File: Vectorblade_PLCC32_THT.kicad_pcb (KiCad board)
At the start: 2 copper layers, 47.2 x 46.9 mm, 12 parts, among them CON3 EDGE-CONNECTOR, U1 SST39SF020, U2 74AHC1G04, U3 74AHC1G08

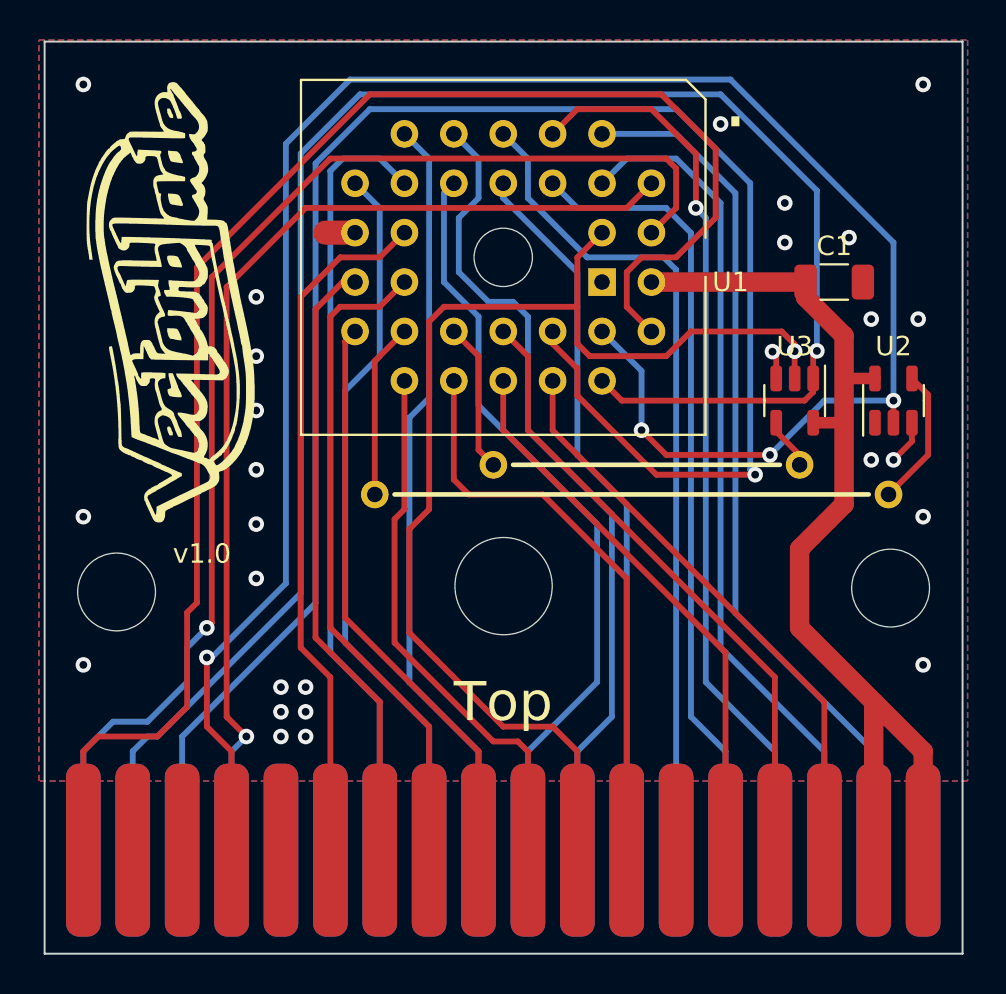
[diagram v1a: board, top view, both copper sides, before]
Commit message: Correct CE error
Correct CE schematic and board error
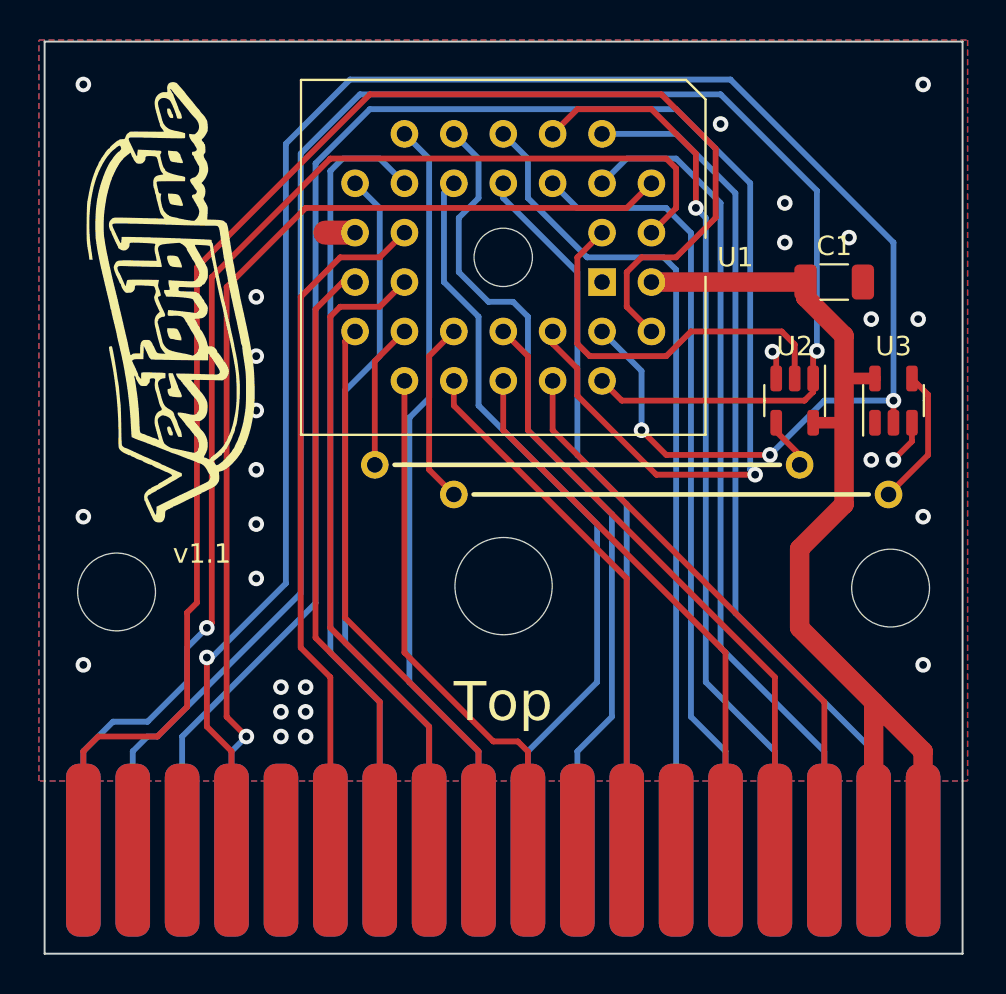
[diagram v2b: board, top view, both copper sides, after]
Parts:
- U2: value 74AHC1G04 -> 74AHC1G08
- U3: value 74AHC1G08 -> 74AHC1G04
- moved U2 5.08 mm to (172.5, 91.2), turned to -90 degrees
- moved U3 5.08 mm to (177.5, 91.2), turned to 90 degrees
- moved ? 2.54 mm to (154.9, 96.0)
- moved ? 1.52 mm to (150.9, 94.5)
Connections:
- ? pad 22: Net-(U1-Pad22) -> /~{CE}
- ? pad 22: Net-(U1-Pad22) -> /~{OE}
- ? pad 24: Net-(U1-Pad24) -> /~{OE}
- ? pad 24: Net-(U1-Pad24) -> /~{CE}
- CON3 pad 16: /V-CE -> unconnected-(CON3-Pad16)
- U1 pad 22: Net-(U1-Pad22) -> /~{CE}
- U1 pad 24: Net-(U1-Pad24) -> /~{OE}
- U1 pad 3: /V-CE -> /V-A15
- U2 pad 1: (no net) -> /V-A14
- U2 pad 2: /V-RW -> /V-A15
- U2 pad 4: Net-(U1-Pad22) -> /~{CE}
- U3 pad 1: /V-A14 -> (no net)
- U3 pad 2: /V-CE -> /V-RW
- U3 pad 4: Net-(U1-Pad24) -> /~{OE}
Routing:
- net /V-CE: track 60.8 -> 0.00 mm, vias 1 -> 0
- net /V-A15: track 0.00 -> 20.2 mm
- net /~{OE}: track 0.00 -> 16.6 mm
- net Net-(U1-Pad22): track 16.2 -> 0.00 mm
- net Net-(U1-Pad24): track 10.7 -> 0.00 mm
- net /~{CE}: track 0.00 -> 10.2 mm
- net /V-A10: track 30.0 -> 27.8 mm
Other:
- board text added: "v1.1"
- board text removed: "."
- board text removed: "v1.0"

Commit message: I forgot to connect A15
Shame !
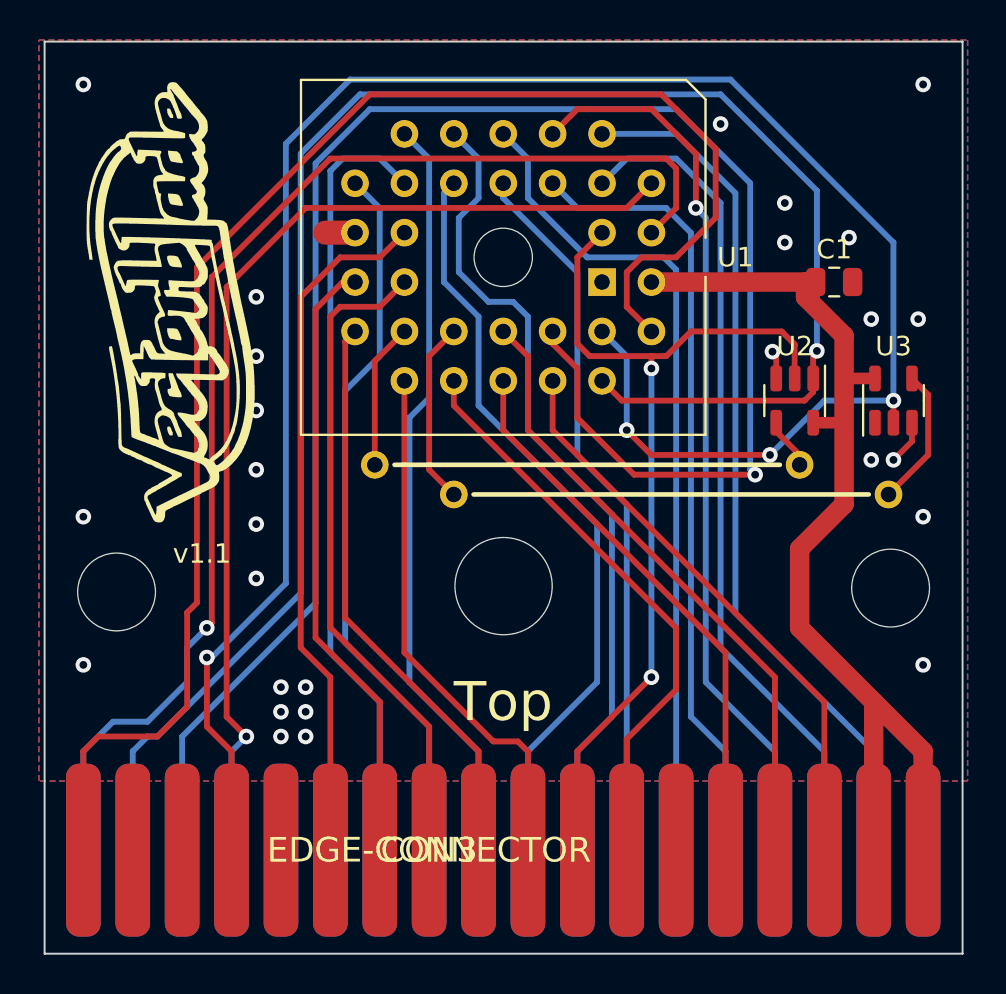
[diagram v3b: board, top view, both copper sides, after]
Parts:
- C1: footprint Capacitor_SMD:C_1206_3216Metric -> Capacitor_SMD:C_0805_2012Metric
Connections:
- CON3 pad 16: unconnected-(CON3-Pad16) -> /V-A15
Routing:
- net /V-A15: track 20.2 -> 47.2 mm, vias 0 -> 2
- net /V-A10: track 27.8 -> 29.9 mm
- net /V-A13: track 93.0 -> 93.7 mm

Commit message: Update Gerber
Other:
- board text added: "v1.2"
- board text removed: "v1.1"
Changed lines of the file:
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@@
     (effects (font (size 2 2) (thickness 0.4)))
   )
-  (gr_text "v1.1" (at 141.986 99.06) (layer "F.SilkS")
+  (gr_text "v1.2" (at 141.986 99.06) (layer "F.SilkS")
     (effects (font (size 1 1) (thickness 0.2)))
   )
@@
   (segment (start 141.224 102.086015) (end 141.224 106.934) (width 0.3) (layer "F.Cu") (net 31))
   (segment (start 166.37 83.82) (end 168.402 81.788) (width 0.3) (layer "F.Cu") (net 31))
-  (segment (start 165.1 89.535) (end 165.1 88.9) (width 0.3) (layer "F.Cu") (net 34))
   (segment (start 167.132 87.63) (end 171.79925 87.63) (width 0.3) (layer "F.Cu") (net 34))
   (segment (start 161.29 83.82) (end 161.29 88.265) (width 0.3) (layer "F.Cu") (net 34))
@@
   (segment (start 172.466 88.29675) (end 172.466 90.0485) (width 0.3) (layer "F.Cu") (net 34))
   (segment (start 165.1 88.9) (end 165.862 88.9) (width 0.3) (layer "F.Cu") (net 34))
+  (segment (start 165.1 89.281) (end 165.1 88.9) (width 0.3) (layer "F.Cu") (net 34))
   (segment (start 165.1 105.41) (end 161.29 109.22) (width 0.3) (layer "F.Cu") (net 34))
   (segment (start 171.79925 87.63) (end 172.466 88.29675) (width 0.3) (layer "F.Cu") (net 34))
@@
   (segment (start 162.56 82.55) (end 161.29 83.82) (width 0.3) (layer "F.Cu") (net 34))
   (via (at 165.1 105.41) (size 0.8) (drill 0.4) (layers "F.Cu" "B.Cu") (net 34))
-  (via (at 165.1 89.535) (size 0.8) (drill 0.4) (layers "F.Cu" "B.Cu") (net 34))
-  (segment (start 165.1 105.41) (end 165.1 89.535) (width 0.3) (layer "B.Cu") (net 34))
+  (via (at 165.1 89.281) (size 0.8) (drill 0.4) (layers "F.Cu" "B.Cu") (net 34))
+  (segment (start 165.1 105.41) (end 165.1 89.281) (width 0.3) (layer "B.Cu") (net 34))
   (segment (start 150.876 89.154) (end 150.876 94.488) (width 0.3) (layer "F.Cu") (net 35))
   (segment (start 152.4 87.63) (end 150.876 89.154) (width 0.3) (layer "F.Cu") (net 35))
